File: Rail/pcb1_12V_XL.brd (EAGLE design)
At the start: 96.3 x 101.8 mm, 116 parts, among them J1 638207222006, J10 638207222006, J11 638207222006, J12 638207222006, J2 638207222006, J4 61302211821, J8 61302211821, U1 ESP32-S3-DEVKITC-1-N8R2, U4 TLE9250VSJ, X2 B4P-VH

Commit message: cleanup
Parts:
- removed D6: 26.2V / 35pF, fliegl-wuerth:WE-TVS_SOT23-3L
- added D11: 24Vdc, Wurth_EMC Components_WE-TVS:WE-TVS_SOT23-3L
- J4, J8: device Eagle_WR-PHD (rev22a):61302211821 -> Wurth_Connectors_WR-PHD:61302211821
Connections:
- net CAN_N: now also D11.1; no longer D6.1
- net CAN_P: now also D11.2; no longer D6.2
- net ECU_GND: now also D11.3; no longer D6.3
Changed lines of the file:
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@@
 <attribute name="VR" value="50V(DC)" x="82.9912" y="119.4" size="1.778" layer="27" rot="R270" display="off"/>
-</element>
-<element name="D6" library="fliegl-wuerth" package="WE-TVS_SOT23-3L" value="26.2V / 35pF" x="80.8388" y="87.4128" smashed="yes" rot="R90">
-<attribute name="ARTIKEL_NR" value="531887" x="73.2188" y="44.2328" size="1.778" layer="27" rot="R90" display="off"/>
-<attribute name="KOMPONENTENNUMMER" value="617684" x="73.2188" y="44.2328" size="1.778" layer="27" rot="R90" display="off"/>
-<attribute name="NAME" x="78.5568" y="87.6078" size="0.8128" layer="25" rot="R90" align="bottom-center"/>
-<attribute name="VALUE" x="83.4908" y="85.8078" size="0.6096" layer="27" rot="R90"/>
-<attribute name="WE-NUMBER" value="824098024" x="73.2188" y="44.2328" size="1.778" layer="27" rot="R90" display="off"/>
 </element>
 <element name="C17" library="Wurth_Capacitors_WCAP-CSGP" library_urn="urn:adsk.eagle:library:18488985" package="WCAP-CSGP_0805_H0.8_R" package3d_urn="urn:adsk.eagle:package:18489119/2" value="100nF" x="53.34" y="64.79" smashed="yes">
@@
 <attribute name="VALUE" x="-0.36" y="71.37" size="1.27" layer="27" rot="R270" align="top-left"/>
 </element>
-<element name="J4" library="Eagle_WR-PHD (rev22a)" package="61302211821" package3d_urn="urn:adsk.eagle:package:14805555/2" value=" 61302211821 " x="45.72" y="125.75" smashed="yes">
+<element name="J4" library="Wurth_Connectors_WR-PHD" library_urn="urn:adsk.eagle:library:14804658" package="61302211821" package3d_urn="urn:adsk.eagle:package:14805555/2" value=" 61302211821 " x="45.72" y="125.75" smashed="yes">
 <attribute name="DATASHEET-URL" value="https://www.we-online.com/redexpert/spec/61302211821?ae" x="15.24" y="195.6" size="1.778" layer="27" display="off"/>
 <attribute name="GENDER" value="Socket Header" x="15.24" y="195.6" size="1.778" layer="27" display="off"/>
@@
 <attribute name="VALUE" x="16.7224" y="124.5558" size="0.8128" layer="27" align="bottom-right"/>
 </element>
-<element name="J8" library="Eagle_WR-PHD (rev22a)" package="61302211821" package3d_urn="urn:adsk.eagle:package:14805555/2" value=" 61302211821 " x="45.72" y="120.67" smashed="yes">
+<element name="J8" library="Wurth_Connectors_WR-PHD" library_urn="urn:adsk.eagle:library:14804658" package="61302211821" package3d_urn="urn:adsk.eagle:package:14805555/2" value=" 61302211821 " x="45.72" y="120.67" smashed="yes">
 <attribute name="DATASHEET-URL" value="https://www.we-online.com/redexpert/spec/61302211821?ae" x="12.7" y="190.52" size="1.778" layer="27" display="off"/>
 <attribute name="GENDER" value="Socket Header" x="12.7" y="190.52" size="1.778" layer="27" display="off"/>
@@
 <attribute name="VBR" value="4.5V" x="38.1" y="60.96" size="1.778" layer="27" rot="R90" display="off"/>
 </element>
+<element name="D11" library="Wurth_EMC Components_WE-TVS" library_urn="urn:adsk.eagle:library:14282971" package="WE-TVS_SOT23-3L" package3d_urn="urn:adsk.eagle:package:12152380/4" value="24Vdc" x="80.858915625" y="87.675475" smashed="yes">
+<attribute name="C-CH" value="38pF" x="80.858915625" y="87.675475" size="1.778" layer="27" display="off"/>
+<attribute name="CHANNELS" value=" 2 " x="80.858915625" y="87.675475" size="1.778" layer="27" display="off"/>
+<attribute name="DATASHEET-URL" value="https://www.we-online.com/catalog/datasheet/824094024.pdf" x="80.858915625" y="87.675475" size="1.778" layer="27" display="off"/>
+<attribute name="IPEAK" value="6A" x="80.858915625" y="87.675475" size="1.778" layer="27" display="off"/>
+<attribute name="MOUNT" value="SMT" x="80.858915625" y="87.675475" size="1.778" layer="27" display="off"/>
+<attribute name="NAME" x="80.858915625" y="89.875475" size="0.8128" layer="25" align="bottom-center"/>
+<attribute name="PART-NUMBER" value=" 824094024 " x="80.858915625" y="87.675475" size="1.778" layer="27" display="off"/>
+<attribute name="VALUE" x="80.858915625" y="84.675475" size="0.8128" layer="27" align="bottom-center"/>
+<attribute name="VBR" value="26.2V" x="80.858915625" y="87.675475" size="1.778" layer="27" display="off"/>
+</element>
 </elements>
 <signals>
@@
 <signal name="CAN_P">
 <contactref element="U4" pad="7"/>
-<contactref element="D6" pad="2"/>
 <contactref element="R1" pad="2"/>
 <contactref element="X2" pad="3"/>
 <wire x1="83.11" y1="93.98" x2="81.7888" y2="92.6588" width="0.1524" layer="1"/>
-<wire x1="81.7888" y1="92.6588" x2="81.7888" y2="86.3628" width="0.1524" layer="1"/>
 <wire x1="54.61" y1="59.69" x2="62.23" y2="59.69" width="0.1524" layer="1"/>
 <wire x1="62.23" y1="59.69" x2="78.58025" y2="76.04025" width="0.1524" layer="1"/>
@@
 <wire x1="53.4924" y1="58.5724" x2="54.61" y2="59.69" width="0.1524" layer="1"/>
 <wire x1="53.4924" y1="57.8324" x2="53.4924" y2="58.5724" width="0.1524" layer="1"/>
-<wire x1="81.7888" y1="86.3628" x2="80.8388" y2="85.4128" width="0.1524" layer="1"/>
-<wire x1="80.8388" y1="85.4128" x2="80.8388" y2="83.48" width="0.1524" layer="1"/>
 <wire x1="80.8388" y1="83.48" x2="80.8388" y2="83.3032875" width="0.1524" layer="1"/>
 <wire x1="80.8388" y1="83.3032875" x2="81.8174" y2="82.3246875" width="0.1524" layer="1"/>
@@
 <wire x1="80.8388" y1="77.4093125" x2="79.4697375" y2="76.04025" width="0.1524" layer="1"/>
 <wire x1="79.4697375" y1="76.04025" x2="78.58025" y2="76.04025" width="0.1524" layer="1"/>
+<contactref element="D11" pad="2"/>
+<wire x1="80.8388" y1="85.655359375" x2="81.808915625" y2="86.625475" width="0.1524" layer="1"/>
+<wire x1="80.8388" y1="83.48" x2="80.8388" y2="85.655359375" width="0.1524" layer="1"/>
+<wire x1="81.7888" y1="92.6588" x2="81.7888" y2="86.645590625" width="0.1524" layer="1"/>
+<wire x1="81.7888" y1="86.645590625" x2="81.808915625" y2="86.625475" width="0.1524" layer="1"/>
 </signal>
 <signal name="CAN_N">
 <contactref element="U4" pad="6"/>
-<contactref element="D6" pad="1"/>
 <contactref element="R3" pad="2"/>
 <wire x1="78.2988" y1="83.48" x2="78.2988" y2="83.82" width="0.254" layer="1"/>
 <contactref element="X2" pad="4"/>
-<wire x1="79.15" y1="93.98" x2="79.8888" y2="93.2412" width="0.1524" layer="1"/>
-<wire x1="79.8888" y1="93.2412" x2="79.8888" y2="86.3628" width="0.1524" layer="1"/>
 <wire x1="62.1037375" y1="59.9948" x2="78.2988" y2="76.1898625" width="0.1524" layer="1"/>
 <wire x1="54.48374375" y1="59.9948" x2="62.1037375" y2="59.9948" width="0.1524" layer="1"/>
@@
 <wire x1="54.48374375" y1="59.9948" x2="54.394475" y2="59.90553125" width="0.1524" layer="1"/>
 <wire x1="54.394475" y1="59.90553125" x2="54.39446875" y2="59.90553125" width="0.1524" layer="1"/>
-<wire x1="79.8888" y1="86.3628" x2="79.8888" y2="85.41" width="0.1524" layer="1"/>
-<wire x1="79.8888" y1="85.41" x2="78.2988" y2="83.82" width="0.1524" layer="1"/>
+<wire x1="79.7894" y1="85.3106" x2="78.2988" y2="83.82" width="0.1524" layer="1"/>
 <wire x1="78.2988" y1="83.48" x2="78.2988" y2="83.3032875" width="0.1524" layer="1"/>
 <wire x1="78.2988" y1="83.3032875" x2="77.3202" y2="82.3246875" width="0.1524" layer="1"/>
@@
 <wire x1="77.3202" y1="80.8353125" x2="78.2988" y2="79.8567125" width="0.1524" layer="1"/>
 <wire x1="78.2988" y1="79.8567125" x2="78.2988" y2="76.1898625" width="0.1524" layer="1"/>
+<contactref element="D11" pad="1"/>
+<wire x1="79.908915625" y1="93.221084375" x2="79.908915625" y2="86.625475" width="0.1524" layer="1"/>
+<wire x1="79.15" y1="93.98" x2="79.908915625" y2="93.221084375" width="0.1524" layer="1"/>
+<wire x1="79.7894" y1="85.3106" x2="79.7894" y2="86.505959375" width="0.1524" layer="1"/>
+<wire x1="79.7894" y1="86.505959375" x2="79.908915625" y2="86.625475" width="0.1524" layer="1"/>
 </signal>
 <signal name="+3V3">
@@
 <contactref element="C10" pad="1"/>
 <contactref element="C15" pad="2"/>
-<contactref element="D6" pad="3"/>
 <contactref element="C17" pad="2"/>
 <contactref element="C19" pad="2"/>
@@
 <contactref element="J2" pad="A5"/>
 <contactref element="J2" pad="5"/>
+<contactref element="D11" pad="3"/>
 </signal>
 <signal name="IX00">
@@
 <mfgpreviewcolor name="substratecolor" color="0xFF786E46"/>
 </mfgpreviewcolors>
-<errors>
-</errors>
 </board>
 </drawing>

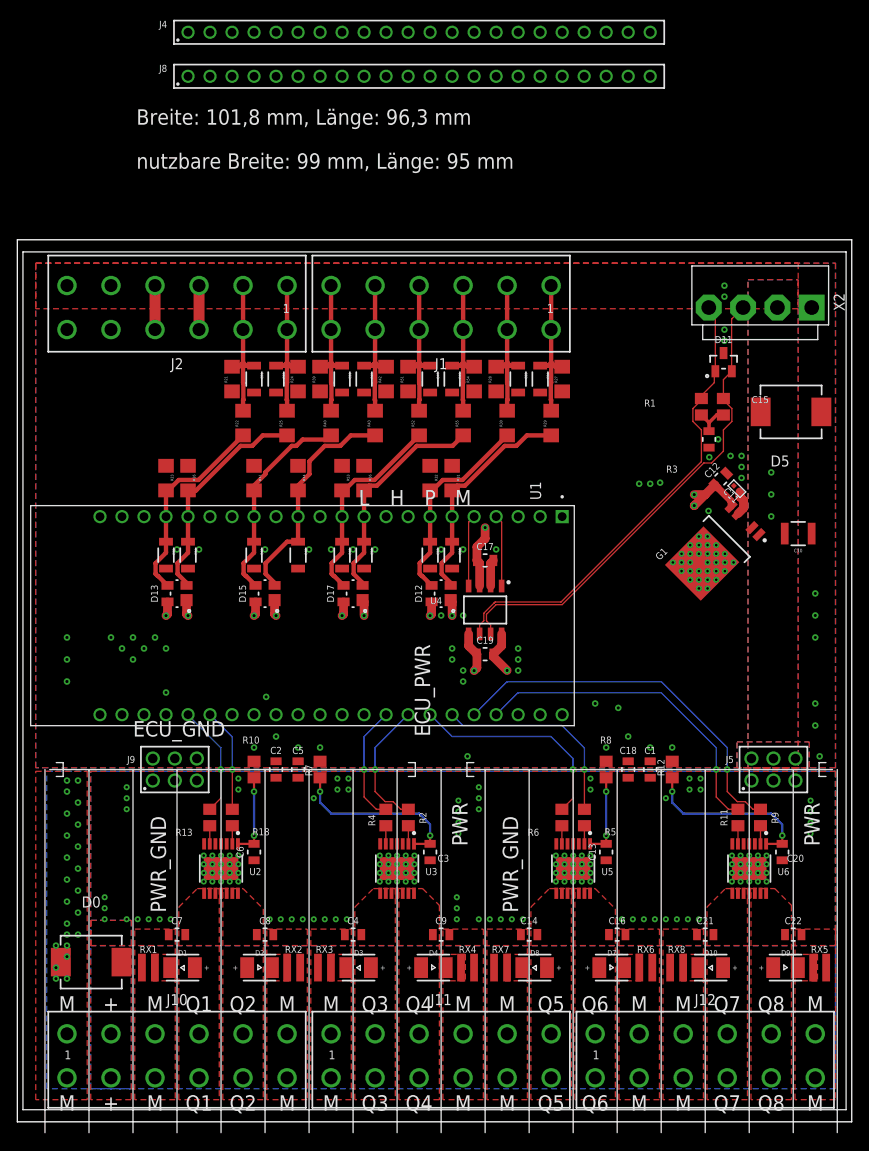
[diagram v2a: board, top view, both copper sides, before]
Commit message: change some Resistors
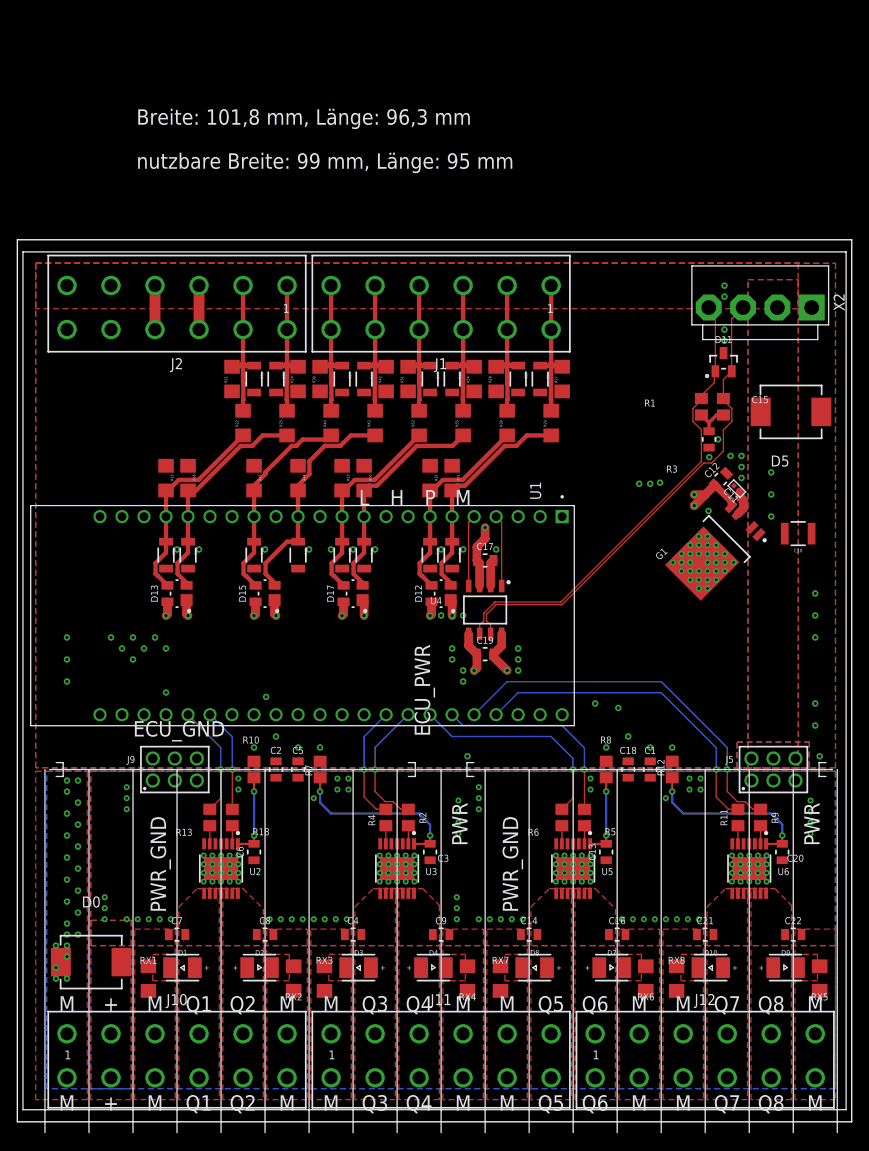
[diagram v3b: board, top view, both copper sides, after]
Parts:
- removed J4, J8: 61302211821, Wurth_Connectors_WR-PHD:61302211821
- RX1, RX2, RX3, RX4, RX5, RX6, RX7, RX8: device Wurth_Resistor_WRIS-KWKB:WRIS-KWKB_0612 -> resistor:R1206
- moved RX1 1.27 mm to (14.5, 16.5)
- moved RX2 1.27 mm to (31.2, 16.5), turned to 270 degrees
- moved RX3 1.27 mm to (34.8, 16.5)
- moved RX4 1.27 mm to (51.3, 16.5), turned to 270 degrees
- moved RX5 1.27 mm to (91.9, 16.5), turned to 270 degrees
- moved RX6 1.27 mm to (71.9, 16.5), turned to 270 degrees
- moved RX7 1.27 mm to (55.1, 16.5)
- moved RX8 1.27 mm to (75.4, 16.5)
